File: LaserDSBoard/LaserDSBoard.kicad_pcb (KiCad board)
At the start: 2 copper layers, 110.5 x 77 mm, 185 parts, among them J1 JTAG, J10 Y LIMIT2, J11 LASER, J12 Y VREF, J13 X VREF, J14 Y1 MOTOR, J15 X MOTOR, J16 Y2 MOTOR, J2 USB, J3 POWER IN, J4 LASER P, J5 D SWITCH, J6 WATER FLOW, J7 X LIMIT1, J8 X LIMIT2, J9 Y LIMIT1, SW1 SW_PUSH, SW2 SWITCH_INV, U1 LD1117S33TR, U10 74HC08A, U11 ADUM1250, U12 TLP2355, U13 TLP2355, U14 TLP2355, U15 TLP2355, U16 TLP2355, U17 TLP2355, U18 74HC1G00, U19 MCP3425, U2 LD1117S33TR, U20 A4982SLPTR, U21 A4982SLPTR, U22 TLP2355, U3 STM32F20XR, U4 LD1117S50TR, U5 ADUM1250, U6 TLP627-4, U7 TLP627, U8 MCP44X1, U9 TLP627, X1 CRYSTAL_4PIN, X2 CRYSTAL

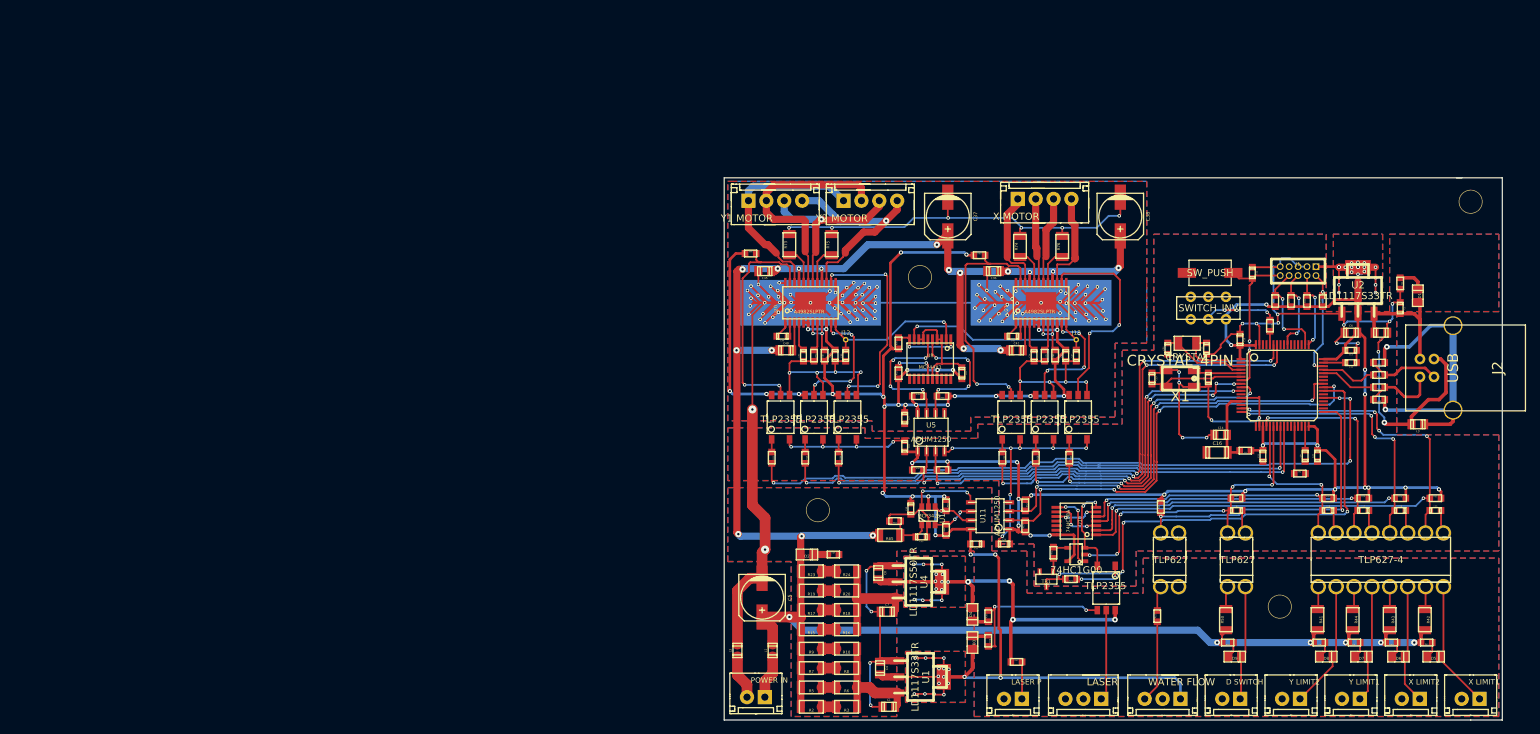
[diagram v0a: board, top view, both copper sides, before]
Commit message: DSコントロール基板改版
・2→4層化
・Y軸モータードライバ増設(1→2)
・コネクタ変更
・デジタルポテンショメータ変更
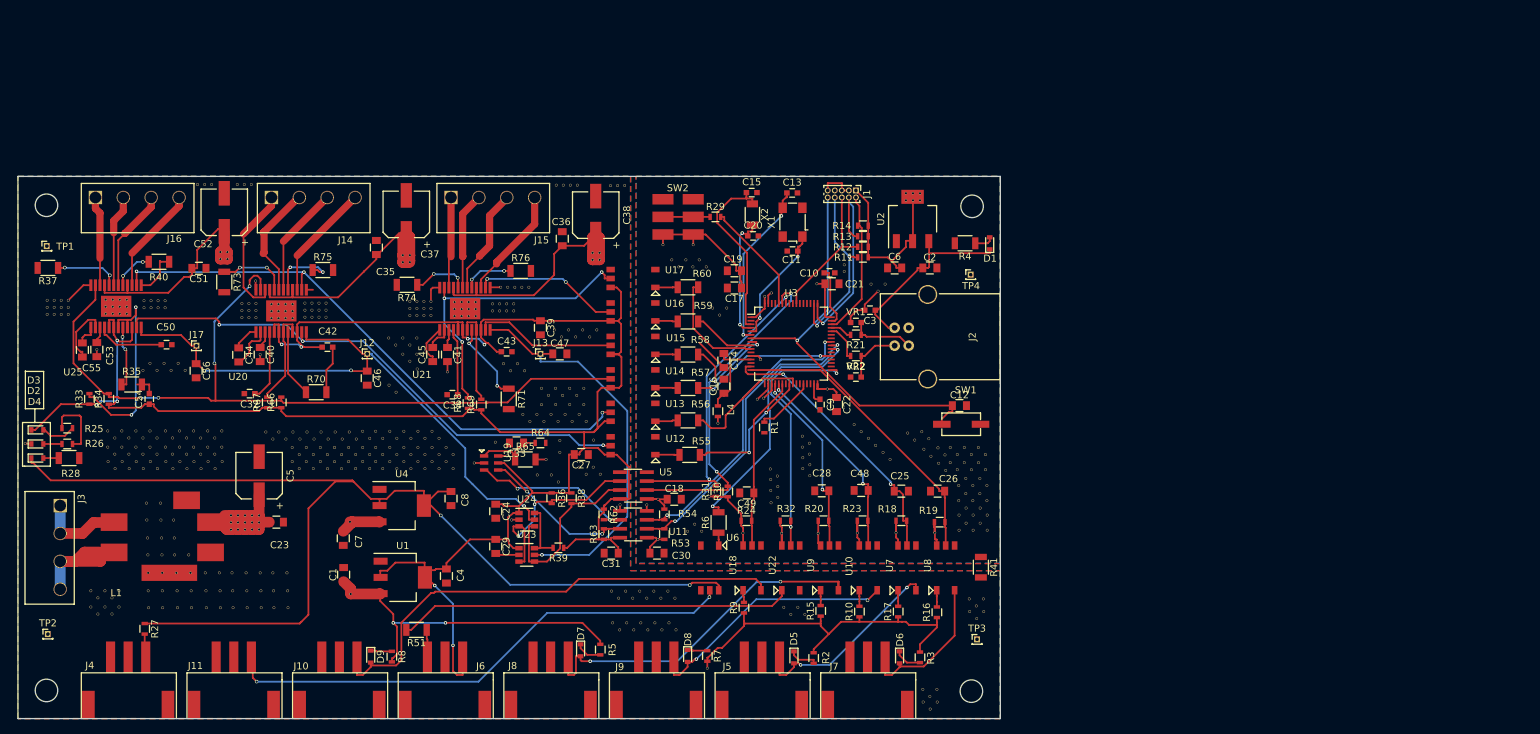
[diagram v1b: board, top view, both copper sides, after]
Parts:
- removed the ? at (245.3, 134.7)
- removed the ? at (338.0, 90.9)
- removed the ? at (310.9, 148.4)
- removed the ? at (259.8, 101.6)
- removed L2: BLM21SN300SN1D, C_0805
- removed L3: BLM21PG221SN1D, C_0805
- removed R42, R43, R44, R50: 1k, R_1206
- removed R45, R46, R47, R48, R49: 4k7, R_0603
- removed R52: 10k, R_0603
- removed R61: 100R, R_0603
- removed R72: 220R, R_0603
- removed TR1: BSH105, SOT-23
- added ?: , mylib:via, F.Cu at (201.2, 127.0)
- added ?: , mylib:via, F.Cu at (154.3, 148.6)
- added ?: , mylib:via, F.Cu at (243.2, 127.2)
- added ?: , mylib:via, F.Cu at (244.2, 128.2)
- added ?: , mylib:via, F.Cu at (244.2, 129.8)
- added ?: , mylib:via, F.Cu at (243.2, 128.8)
- added ?: , mylib:via, F.Cu at (243.1, 125.8)
- added ?: , mylib:via, F.Cu at (244.1, 126.8)
- added ?: , mylib:via, F.Cu at (254.6, 126.5)
- added ?: , mylib:via, F.Cu at (255.6, 127.5)
- added ?: , mylib:via, F.Cu at (253.5, 125.5)
- added ?: , mylib:via, F.Cu at (252.5, 124.5)
- added ?: , mylib:via, F.Cu at (156.3, 148.6)
- added ?: , mylib:via, F.Cu at (250.4, 122.5)
- added ?: , mylib:via, F.Cu at (251.4, 123.5)
- added ?: , mylib:via, F.Cu at (266.4, 136.6)
- added ?: , mylib:via, F.Cu at (268.4, 136.6)
- added ?: , mylib:via, F.Cu at (265.4, 137.6)
- added ?: , mylib:via, F.Cu at (267.4, 137.6)
- added ?: , mylib:via, F.Cu at (269.4, 137.6)
- added ?: , mylib:via, F.Cu at (269.4, 135.4)
- added ?: , mylib:via, F.Cu at (267.4, 135.4)
- added ?: , mylib:via, F.Cu at (265.4, 135.4)
- added ?: , mylib:via, F.Cu at (156.3, 146.2)
- added ?: , mylib:via, F.Cu at (268.4, 134.4)
- added ?: , mylib:via, F.Cu at (266.4, 134.4)
- added ?: , mylib:via, F.Cu at (266.3, 130.2)
- added ?: , mylib:via, F.Cu at (268.3, 130.2)
- added ?: , mylib:via, F.Cu at (265.3, 131.2)
- added ?: , mylib:via, F.Cu at (267.3, 131.2)
- added ?: , mylib:via, F.Cu at (269.3, 131.2)
- added ?: , mylib:via, F.Cu at (269.3, 133.3)
- added ?: , mylib:via, F.Cu at (267.3, 133.3)
- added ?: , mylib:via, F.Cu at (265.3, 133.3)
- added ?: , mylib:via, F.Cu at (154.3, 146.2)
- added ?: , mylib:via, F.Cu at (268.3, 132.3)
- added ?: , mylib:via, F.Cu at (266.3, 132.3)
- added ?: , mylib:via, F.Cu at (261.1, 124.5)
- added ?: , mylib:via, F.Cu at (244.1, 125.2)
- added ?: , mylib:via, F.Cu at (260.1, 123.5)
- added ?: , mylib:via, F.Cu at (243.1, 124.2)
- added ?: , mylib:via, F.Cu at (230.3, 106.0)
- added ?: , mylib:via, F.Cu at (232.3, 106.0)
- added ?: , mylib:via, F.Cu at (231.3, 107.0)
- added ?: , mylib:via, F.Cu at (228.4, 99.2)
- added ?: , mylib:via, F.Cu at (150.2, 146.2)
- added ?: , mylib:via, F.Cu at (229.4, 100.2)
- added ?: , mylib:via, F.Cu at (227.6, 100.2)
- added ?: , mylib:via, F.Cu at (225.6, 100.2)
- added ?: , mylib:via, F.Cu at (226.6, 99.2)
- added ?: , mylib:via, F.Cu at (224.6, 99.2)
- added ?: , mylib:via, F.Cu at (237.2, 113.3)
- added ?: , mylib:via, F.Cu at (263.4, 129.1)
- added ?: , mylib:via, F.Cu at (262.4, 128.1)
- added ?: , mylib:via, F.Cu at (227.8, 136.7)
- added ?: , mylib:via, F.Cu at (226.8, 137.7)
- added ?: , mylib:via, F.Cu at (152.2, 146.2)
- added ?: , mylib:via, F.Cu at (228.8, 137.7)
- added ?: , mylib:via, F.Cu at (264.1, 128.0)
- added ?: , mylib:via, F.Cu at (266.1, 128.0)
- added ?: , mylib:via, F.Cu at (268.1, 128.0)
- added ?: , mylib:via, F.Cu at (265.1, 128.9)
- added ?: , mylib:via, F.Cu at (267.1, 128.9)
- added ?: , mylib:via, F.Cu at (269.1, 128.9)
- added ?: , mylib:via, F.Cu at (249.1, 100.8)
- added ?: , mylib:via, F.Cu at (249.1, 99.8)
- added ?: , mylib:via, F.Cu at (252.8, 102.6)
- added ?: , mylib:via, F.Cu at (152.2, 148.6)
- added ?: , mylib:via, F.Cu at (254.8, 102.6)
- added ?: , mylib:via, F.Cu at (253.8, 103.6)
- added ?: , mylib:via, F.Cu at (238.7, 103.8)
- added ?: , mylib:via, F.Cu at (193.5, 128.8)
- added ?: , mylib:via, F.Cu at (191.5, 128.8)
- added ?: , mylib:via, F.Cu at (189.5, 128.8)
- added ?: , mylib:via, F.Cu at (187.5, 128.8)
- added ?: , mylib:via, F.Cu at (185.5, 128.8)
- added ?: , mylib:via, F.Cu at (183.5, 128.8)
- added ?: , mylib:via, F.Cu at (192.5, 127.8)
- added ?: , mylib:via, F.Cu at (150.2, 148.6)
- added ?: , mylib:via, F.Cu at (190.5, 127.8)
- added ?: , mylib:via, F.Cu at (188.5, 127.8)
- added ?: , mylib:via, F.Cu at (186.5, 127.8)
- added ?: , mylib:via, F.Cu at (184.5, 127.8)
- added ?: , mylib:via, F.Cu at (182.5, 127.8)
- added ?: , mylib:via, F.Cu at (170.7, 127.8)
- added ?: , mylib:via, F.Cu at (172.7, 127.8)
- added ?: , mylib:via, F.Cu at (174.7, 127.8)
- added ?: , mylib:via, F.Cu at (176.7, 127.8)
- added ?: , mylib:via, F.Cu at (178.7, 127.8)
- added ?: , mylib:via, F.Cu at (168.1, 148.6)
- added ?: , mylib:via, F.Cu at (180.7, 127.8)
- added ?: , mylib:via, F.Cu at (171.7, 128.8)
- added ?: , mylib:via, F.Cu at (173.7, 128.8)
- added ?: , mylib:via, F.Cu at (175.7, 128.8)
- added ?: , mylib:via, F.Cu at (177.7, 128.8)
- added ?: , mylib:via, F.Cu at (179.7, 128.8)
- added ?: , mylib:via, F.Cu at (181.7, 128.8)
- added ?: , mylib:via, F.Cu at (168.8, 123.6)
- added ?: , mylib:via, F.Cu at (170.8, 123.6)
- added ?: , mylib:via, F.Cu at (172.8, 123.6)
- added ?: , mylib:via, F.Cu at (170.1, 148.6)
- added ?: , mylib:via, F.Cu at (174.8, 123.6)
- added ?: , mylib:via, F.Cu at (176.8, 123.6)
- added ?: , mylib:via, F.Cu at (178.8, 123.6)
- added ?: , mylib:via, F.Cu at (169.8, 124.6)
- added ?: , mylib:via, F.Cu at (171.8, 124.6)
- added ?: , mylib:via, F.Cu at (173.8, 124.6)
- added ?: , mylib:via, F.Cu at (175.8, 124.6)
- added ?: , mylib:via, F.Cu at (177.8, 124.6)
- added ?: , mylib:via, F.Cu at (179.8, 124.6)
- added ?: , mylib:via, F.Cu at (167.9, 124.6)
- added ?: , mylib:via, F.Cu at (196.5, 128.0)
- added ?: , mylib:via, F.Cu at (170.0, 146.2)
- added ?: , mylib:via, F.Cu at (166.9, 123.6)
- added ?: , mylib:via, F.Cu at (213.4, 124.8)
- added ?: , mylib:via, F.Cu at (208.7, 124.8)
- added ?: , mylib:via, F.Cu at (208.7, 126.5)
- added ?: , mylib:via, F.Cu at (208.4, 130.7)
- added ?: , mylib:via, F.Cu at (201.8, 136.1)
- added ?: , mylib:via, F.Cu at (207.4, 129.7)
- added ?: , mylib:via, F.Cu at (205.4, 129.7)
- added ?: , mylib:via, F.Cu at (211.4, 128.6)
- added ?: , mylib:via, F.Cu at (213.4, 128.6)
- added ?: , mylib:via, F.Cu at (168.0, 146.2)
- added ?: , mylib:via, F.Cu at (212.4, 129.6)
- added ?: , mylib:via, F.Cu at (214.4, 129.6)
- added ?: , mylib:via, F.Cu at (203.7, 114.9)
- added ?: , mylib:via, F.Cu at (201.7, 114.9)
- added ?: , mylib:via, F.Cu at (202.7, 113.9)
- added ?: , mylib:via, F.Cu at (200.7, 113.9)
- added ?: , mylib:via, F.Cu at (207.9, 109.1)
- added ?: , mylib:via, F.Cu at (209.9, 109.1)
- added ?: , mylib:via, F.Cu at (211.9, 109.1)
- added ?: , mylib:via, F.Cu at (213.9, 109.1)
- added ?: , mylib:via, F.Cu at (169.9, 143.6)
- added ?: , mylib:via, F.Cu at (208.9, 110.1)
- added ?: , mylib:via, F.Cu at (210.9, 110.1)
- added ?: , mylib:via, F.Cu at (212.9, 110.1)
- added ?: , mylib:via, F.Cu at (266.9, 149.1)
- added ?: , mylib:via, F.Cu at (268.9, 149.1)
- added ?: , mylib:via, F.Cu at (267.9, 150.1)
- added ?: , mylib:via, F.Cu at (267.8, 148.3)
- added ?: , mylib:via, F.Cu at (268.8, 147.3)
- added ?: , mylib:via, F.Cu at (266.8, 147.3)
- added ?: , mylib:via, F.Cu at (260.2, 160.2)
- added ?: , mylib:via, F.Cu at (167.9, 143.6)
- added ?: , mylib:via, F.Cu at (262.2, 160.2)
- added ?: , mylib:via, F.Cu at (261.2, 161.2)
- added ?: , mylib:via, F.Cu at (261.2, 162.9)
- added ?: , mylib:via, F.Cu at (262.2, 161.9)
- added ?: , mylib:via, F.Cu at (260.2, 161.9)
- added ?: , mylib:via, F.Cu at (225.0, 147.2)
- added ?: , mylib:via, F.Cu at (223.0, 147.2)
- added ?: , mylib:via, F.Cu at (221.0, 147.2)
- added ?: , mylib:via, F.Cu at (219.0, 147.2)
- added ?: , mylib:via, F.Cu at (217.0, 147.2)
- added ?: , mylib:via, F.Cu at (166.1, 143.6)
- added ?: , mylib:via, F.Cu at (224.0, 146.2)
- added ?: , mylib:via, F.Cu at (222.0, 146.2)
- added ?: , mylib:via, F.Cu at (220.0, 146.2)
- added ?: , mylib:via, F.Cu at (218.0, 146.2)
- added ?: , mylib:via, F.Cu at (216.0, 146.2)
- added ?: , mylib:via, F.Cu at (212.4, 122.1)
- added ?: , mylib:via, F.Cu at (210.4, 122.1)
- added ?: , mylib:via, F.Cu at (208.4, 122.1)
- added ?: , mylib:via, F.Cu at (206.4, 122.1)
- added ?: , mylib:via, F.Cu at (204.4, 122.1)
- added ?: , mylib:via, F.Cu at (166.2, 146.2)
- added ?: , mylib:via, F.Cu at (211.4, 121.1)
- added ?: , mylib:via, F.Cu at (209.4, 121.1)
- added ?: , mylib:via, F.Cu at (207.4, 121.1)
- added ?: , mylib:via, F.Cu at (205.4, 121.1)
- added ?: , mylib:via, F.Cu at (203.4, 121.1)
- added ?: , mylib:via, F.Cu at (206.1, 119.7)
- added ?: , mylib:via, F.Cu at (208.1, 119.7)
- added ?: , mylib:via, F.Cu at (210.1, 119.7)
- added ?: , mylib:via, F.Cu at (212.1, 119.7)
- added ?: , mylib:via, F.Cu at (211.1, 118.4)
- added ?: , mylib:via, F.Cu at (166.2, 148.6)
- added ?: , mylib:via, F.Cu at (209.1, 118.4)
- added ?: , mylib:via, F.Cu at (207.1, 118.4)
- added ?: , mylib:via, F.Cu at (212.1, 117.4)
- added ?: , mylib:via, F.Cu at (210.1, 117.4)
- added ?: , mylib:via, F.Cu at (208.1, 117.4)
- added ?: , mylib:via, F.Cu at (206.1, 117.4)
- added ?: , mylib:via, F.Cu at (144.4, 123.5)
- added ?: , mylib:via, F.Cu at (146.4, 123.5)
- added ?: , mylib:via, F.Cu at (148.4, 123.5)
- added ?: , mylib:via, F.Cu at (150.4, 123.5)
- added ?: , mylib:via, F.Cu at (158.4, 148.6)
- added ?: , mylib:via, F.Cu at (145.4, 124.5)
- added ?: , mylib:via, F.Cu at (147.4, 124.5)
- added ?: , mylib:via, F.Cu at (149.4, 124.5)
- added ?: , mylib:via, F.Cu at (151.4, 124.5)
- added ?: , mylib:via, F.Cu at (151.4, 126.8)
- added ?: , mylib:via, F.Cu at (149.4, 126.8)
- added ?: , mylib:via, F.Cu at (147.4, 126.8)
- added ?: , mylib:via, F.Cu at (145.4, 126.8)
- added ?: , mylib:via, F.Cu at (150.4, 125.8)
- added ?: , mylib:via, F.Cu at (148.4, 125.8)
- added ?: , mylib:via, F.Cu at (160.4, 148.6)
- added ?: , mylib:via, F.Cu at (146.4, 125.8)
- added ?: , mylib:via, F.Cu at (144.4, 125.8)
- added ?: , mylib:via, F.Cu at (156.2, 143.6)
- added ?: , mylib:via, F.Cu at (154.2, 143.6)
- added ?: , mylib:via, F.Cu at (152.2, 143.6)
- added ?: , mylib:via, F.Cu at (150.2, 143.6)
- added ?: , mylib:via, F.Cu at (142.1, 148.4)
- added ?: , mylib:via, F.Cu at (144.1, 148.4)
- added ?: , mylib:via, F.Cu at (146.1, 148.4)
- added ?: , mylib:via, F.Cu at (143.1, 149.4)
- added ?: , mylib:via, F.Cu at (160.4, 146.2)
- added ?: , mylib:via, F.Cu at (145.1, 149.4)
- added ?: , mylib:via, F.Cu at (145.1, 147.2)
- added ?: , mylib:via, F.Cu at (143.1, 147.2)
- added ?: , mylib:via, F.Cu at (146.1, 146.2)
- added ?: , mylib:via, F.Cu at (144.1, 146.2)
- added ?: , mylib:via, F.Cu at (142.1, 146.2)
- added ?: , mylib:via, F.Cu at (152.7, 125.8)
- added ?: , mylib:via, F.Cu at (154.7, 125.8)
- added ?: , mylib:via, F.Cu at (156.7, 125.8)
- added ?: , mylib:via, F.Cu at (158.7, 125.8)
- added ?: , mylib:via, F.Cu at (199.5, 125.0)
- added ?: , mylib:via, F.Cu at (158.4, 146.2)
- added ?: , mylib:via, F.Cu at (160.7, 125.8)
- added ?: , mylib:via, F.Cu at (153.7, 126.8)
- added ?: , mylib:via, F.Cu at (155.7, 126.8)
- added ?: , mylib:via, F.Cu at (157.7, 126.8)
- added ?: , mylib:via, F.Cu at (159.7, 126.8)
- added ?: , mylib:via, F.Cu at (159.7, 124.5)
- added ?: , mylib:via, F.Cu at (157.7, 124.5)
- added ?: , mylib:via, F.Cu at (155.7, 124.5)
- added ?: , mylib:via, F.Cu at (153.7, 124.5)
- added ?: , mylib:via, F.Cu at (160.7, 123.5)
- added ?: , mylib:via, F.Cu at (160.3, 143.6)
- added ?: , mylib:via, F.Cu at (158.7, 123.5)
- added ?: , mylib:via, F.Cu at (156.7, 123.5)
- added ?: , mylib:via, F.Cu at (154.7, 123.5)
- added ?: , mylib:via, F.Cu at (152.7, 123.5)
- added ?: , mylib:via, F.Cu at (184.3, 110.2)
- added ?: , mylib:via, F.Cu at (186.3, 110.2)
- added ?: , mylib:via, F.Cu at (188.3, 110.2)
- added ?: , mylib:via, F.Cu at (185.3, 111.2)
- added ?: , mylib:via, F.Cu at (187.3, 111.2)
- added ?: , mylib:via, F.Cu at (187.3, 113.5)
- added ?: , mylib:via, F.Cu at (158.3, 143.6)
- added ?: , mylib:via, F.Cu at (188.3, 112.5)
- added ?: , mylib:via, F.Cu at (186.3, 112.5)
- added ?: , mylib:via, F.Cu at (184.4, 117.0)
- added ?: , mylib:via, F.Cu at (185.4, 118.0)
- added ?: , mylib:via, F.Cu at (188.4, 114.7)
- added ?: , mylib:via, F.Cu at (216.2, 150.7)
- added ?: , mylib:via, F.Cu at (218.2, 150.7)
- added ?: , mylib:via, F.Cu at (220.2, 150.7)
- added ?: , mylib:via, F.Cu at (222.2, 150.7)
- added ?: , mylib:via, F.Cu at (224.2, 150.7)
- added ?: , mylib:via, F.Cu at (162.1, 143.6)
- added ?: , mylib:via, F.Cu at (180.7, 123.5)
- added ?: , mylib:via, F.Cu at (217.2, 151.7)
- added ?: , mylib:via, F.Cu at (219.2, 151.7)
- added ?: , mylib:via, F.Cu at (221.2, 151.7)
- added ?: , mylib:via, F.Cu at (223.2, 151.7)
- added ?: , mylib:via, F.Cu at (225.2, 151.7)
- added ?: , mylib:via, F.Cu at (181.7, 124.5)
- added ?: , mylib:via, F.Cu at (181.7, 126.8)
- added ?: , mylib:via, F.Cu at (179.7, 126.8)
- added ?: , mylib:via, F.Cu at (177.7, 126.8)
- added ?: , mylib:via, F.Cu at (164.1, 143.6)
- added ?: , mylib:via, F.Cu at (175.7, 126.8)
- added ?: , mylib:via, F.Cu at (173.7, 126.8)
- added ?: , mylib:via, F.Cu at (171.7, 126.8)
- added ?: , mylib:via, F.Cu at (180.7, 125.8)
- added ?: , mylib:via, F.Cu at (178.7, 125.8)
- added ?: , mylib:via, F.Cu at (176.7, 125.8)
- added ?: , mylib:via, F.Cu at (174.7, 125.8)
- added ?: , mylib:via, F.Cu at (172.7, 125.8)
- added ?: , mylib:via, F.Cu at (170.7, 125.8)
- added ?: , mylib:via, F.Cu at (182.5, 125.8)
- added ?: , mylib:via, F.Cu at (162.2, 146.2)
- added ?: , mylib:via, F.Cu at (184.5, 125.8)
- added ?: , mylib:via, F.Cu at (186.5, 125.8)
- added ?: , mylib:via, F.Cu at (188.5, 125.8)
- added ?: , mylib:via, F.Cu at (190.5, 125.8)
- added ?: , mylib:via, F.Cu at (192.5, 125.8)
- added ?: , mylib:via, F.Cu at (183.5, 126.8)
- added ?: , mylib:via, F.Cu at (185.5, 126.8)
- added ?: , mylib:via, F.Cu at (187.5, 126.8)
- added ?: , mylib:via, F.Cu at (189.5, 126.8)
- added ?: , mylib:via, F.Cu at (191.5, 126.8)
- added ?: , mylib:via, F.Cu at (164.2, 146.2)
- added ?: , mylib:via, F.Cu at (193.5, 126.8)
- added ?: , mylib:via, F.Cu at (151.4, 114.8)
- added ?: , mylib:via, F.Cu at (191.5, 124.5)
- added ?: , mylib:via, F.Cu at (189.5, 124.5)
- added ?: , mylib:via, F.Cu at (187.5, 124.5)
- added ?: , mylib:via, F.Cu at (185.5, 124.5)
- added ?: , mylib:via, F.Cu at (183.5, 124.5)
- added ?: , mylib:via, F.Cu at (155.4, 114.8)
- added ?: , mylib:via, F.Cu at (153.4, 114.8)
- added ?: , mylib:via, F.Cu at (149.4, 114.8)
- added ?: , mylib:via, F.Cu at (164.2, 148.6)
- added ?: , mylib:via, F.Cu at (190.5, 123.5)
- added ?: , mylib:via, F.Cu at (188.5, 123.5)
- added ?: , mylib:via, F.Cu at (186.5, 123.5)
- added ?: , mylib:via, F.Cu at (184.5, 123.5)
- added ?: , mylib:via, F.Cu at (182.5, 123.5)
- added ?: , mylib:via, F.Cu at (154.4, 113.8)
- added ?: , mylib:via, F.Cu at (152.4, 113.8)
- added ?: , mylib:via, F.Cu at (150.4, 113.8)
- added ?: , mylib:via, F.Cu at (259.8, 90.7)
- added ?: , mylib:via, F.Cu at (258.8, 90.7)
- added ?: , mylib:via, F.Cu at (162.2, 148.6)
- added ?: , mylib:via, F.Cu at (257.8, 90.7)
- added ?: , mylib:via, F.Cu at (246.7, 117.5)
- added ?: , mylib:via, F.Cu at (245.2, 102.5)
- added ?: , mylib:via, F.Cu at (229.8, 132.8)
- added ?: , mylib:via, F.Cu at (222.6, 133.2)
- added ?: , mylib:via, F.Cu at (261.9, 137.9)
- added ?: , mylib:via, F.Cu at (250.9, 137.9)
- added ?: , mylib:via, F.Cu at (259.8, 89.7)
- added ?: , mylib:via, F.Cu at (258.8, 89.7)
- added ?: , mylib:via, F.Cu at (257.8, 89.7)
- added ?: , mylib:via, F.Cu at (153.9, 141.1)
- added ?: , mylib:via, F.Cu at (237.6, 118.8)
- added ?: , mylib:via, F.Cu at (231.1, 122.3)
- added ?: , mylib:via, F.Cu at (237.8, 104.3)
- added ?: , mylib:via, F.Cu at (227.6, 97.0)
- added ?: , mylib:via, F.Cu at (223.3, 97.0)
- added ?: , mylib:via, F.Cu at (222.6, 138.8)
- added ?: , mylib:via, F.Cu at (256.4, 137.9)
- added ?: , mylib:via, F.Cu at (245.3, 138.0)
- added ?: , mylib:via, F.Cu at (240.2, 138.0)
- added ?: , mylib:via, F.Cu at (234.7, 137.9)
- added ?: , mylib:via, F.Cu at (161.9, 135.4)
- added ?: , mylib:via, F.Cu at (155.9, 141.1)
- added ?: , mylib:via, F.Cu at (221.0, 133.9)
- added ?: , mylib:via, F.Cu at (236.7, 119.0)
- added ?: , mylib:via, F.Cu at (269.1, 126.8)
- added ?: , mylib:via, F.Cu at (267.1, 126.8)
- added ?: , mylib:via, F.Cu at (265.1, 126.8)
- added ?: , mylib:via, F.Cu at (268.1, 125.8)
- added ?: , mylib:via, F.Cu at (266.1, 125.8)
- added ?: , mylib:via, F.Cu at (187.3, 99.5)
- added ?: , mylib:via, F.Cu at (186.3, 99.5)
- added ?: , mylib:via, F.Cu at (214.3, 99.2)
- added ?: , mylib:via, F.Cu at (153.9, 138.7)
- added ?: , mylib:via, F.Cu at (213.3, 99.2)
- added ?: , mylib:via, F.Cu at (165.9, 137.4)
- added ?: , mylib:via, F.Cu at (164.9, 137.4)
- added ?: , mylib:via, F.Cu at (163.9, 137.4)
- added ?: , mylib:via, F.Cu at (132.8, 125.2)
- added ?: , mylib:via, F.Cu at (161.4, 99.0)
- added ?: , mylib:via, F.Cu at (160.4, 99.0)
- added ?: , mylib:via, F.Cu at (187.3, 98.5)
- added ?: , mylib:via, F.Cu at (186.3, 98.5)
- added ?: , mylib:via, F.Cu at (214.3, 98.2)
- added ?: , mylib:via, F.Cu at (153.8, 136.1)
- added ?: , mylib:via, F.Cu at (213.3, 98.2)
- added ?: , mylib:via, F.Cu at (165.9, 136.4)
- added ?: , mylib:via, F.Cu at (164.9, 136.4)
- added ?: , mylib:via, F.Cu at (163.9, 136.4)
- added ?: , mylib:via, F.Cu at (142.9, 111.9)
- added ?: , mylib:via, F.Cu at (166.1, 112.6)
- added ?: , mylib:via, F.Cu at (192.7, 115.0)
- added ?: , mylib:via, F.Cu at (161.4, 98.0)
- added ?: , mylib:via, F.Cu at (160.4, 98.0)
- added ?: , mylib:via, F.Cu at (178.9, 146.6)
- added ?: , mylib:via, F.Cu at (150.0, 136.1)
- added ?: , mylib:via, F.Cu at (206.7, 127.5)
- added ?: , mylib:via, F.Cu at (178.8, 136.3)
- added ?: , mylib:via, F.Cu at (229.6, 157.2)
- added ?: , mylib:via, F.Cu at (165.9, 135.4)
- added ?: , mylib:via, F.Cu at (164.9, 135.4)
- added ?: , mylib:via, F.Cu at (163.9, 135.4)
- added ?: , mylib:via, F.Cu at (202.1, 106.4)
- added ?: , mylib:via, F.Cu at (201.1, 106.4)
- added ?: , mylib:via, F.Cu at (200.1, 106.4)
- added ?: , mylib:via, F.Cu at (199.1, 106.4)
- added ?: , mylib:via, F.Cu at (152.0, 136.1)
- added ?: , mylib:via, F.Cu at (190.3, 107.0)
- added ?: , mylib:via, F.Cu at (189.3, 107.0)
- added ?: , mylib:via, F.Cu at (188.3, 107.0)
- added ?: , mylib:via, F.Cu at (187.3, 107.0)
- added ?: , mylib:via, F.Cu at (175.4, 107.3)
- added ?: , mylib:via, F.Cu at (174.4, 107.3)
- added ?: , mylib:via, F.Cu at (173.4, 107.3)
- added ?: , mylib:via, F.Cu at (172.4, 107.3)
- added ?: , mylib:via, F.Cu at (165.5, 107.3)
- added ?: , mylib:via, F.Cu at (164.5, 107.3)
- added ?: , mylib:via, F.Cu at (151.9, 133.7)
- added ?: , mylib:via, F.Cu at (163.5, 107.3)
- added ?: , mylib:via, F.Cu at (204.2, 103.0)
- added ?: , mylib:via, F.Cu at (203.2, 103.0)
- added ?: , mylib:via, F.Cu at (202.2, 103.0)
- added ?: , mylib:via, F.Cu at (201.2, 103.0)
- added ?: , mylib:via, F.Cu at (200.2, 103.0)
- added ?: , mylib:via, F.Cu at (202.1, 105.4)
- added ?: , mylib:via, F.Cu at (201.1, 105.4)
- added ?: , mylib:via, F.Cu at (200.1, 105.4)
- added ?: , mylib:via, F.Cu at (199.1, 105.4)
- added ?: , mylib:via, F.Cu at (149.9, 133.7)
- added ?: , mylib:via, F.Cu at (190.3, 106.0)
- added ?: , mylib:via, F.Cu at (189.3, 106.0)
- added ?: , mylib:via, F.Cu at (188.3, 106.0)
- added ?: , mylib:via, F.Cu at (187.3, 106.0)
- added ?: , mylib:via, F.Cu at (175.4, 106.3)
- added ?: , mylib:via, F.Cu at (174.4, 106.3)
- added ?: , mylib:via, F.Cu at (173.4, 106.3)
- added ?: , mylib:via, F.Cu at (172.4, 106.3)
- added ?: , mylib:via, F.Cu at (165.5, 106.3)
- added ?: , mylib:via, F.Cu at (164.5, 106.3)
- added ?: , mylib:via, F.Cu at (150.1, 138.7)
- added ?: , mylib:via, F.Cu at (163.5, 106.3)
- added ?: , mylib:via, F.Cu at (264.1, 125.8)
- added ?: , mylib:via, F.Cu at (190.3, 105.0)
- added ?: , mylib:via, F.Cu at (189.3, 105.0)
- added ?: , mylib:via, F.Cu at (188.3, 105.0)
- added ?: , mylib:via, F.Cu at (187.3, 105.0)
- added ?: , mylib:via, F.Cu at (175.4, 105.3)
- added ?: , mylib:via, F.Cu at (174.4, 105.3)
- added ?: , mylib:via, F.Cu at (173.4, 105.3)
- added ?: , mylib:via, F.Cu at (172.4, 105.3)
- added ?: , mylib:via, F.Cu at (152.1, 138.7)
- added ?: , mylib:via, F.Cu at (165.5, 105.3)
- added ?: , mylib:via, F.Cu at (164.5, 105.3)
- added ?: , mylib:via, F.Cu at (163.5, 105.3)
- added ?: , mylib:via, F.Cu at (138.8, 106.9)
- added ?: , mylib:via, F.Cu at (137.8, 106.9)
- added ?: , mylib:via, F.Cu at (136.8, 106.9)
- added ?: , mylib:via, F.Cu at (135.8, 106.9)
- added ?: , mylib:via, F.Cu at (196.7, 107.2)
- added ?: , mylib:via, F.Cu at (195.7, 107.2)
- added ?: , mylib:via, F.Cu at (194.7, 107.2)
- added ?: , mylib:via, F.Cu at (152.2, 141.1)
- added ?: , mylib:via, F.Cu at (193.7, 107.2)
- added ?: , mylib:via, F.Cu at (170.7, 107.5)
- added ?: , mylib:via, F.Cu at (169.7, 107.5)
- added ?: , mylib:via, F.Cu at (168.7, 107.5)
- added ?: , mylib:via, F.Cu at (167.7, 107.5)
- added ?: , mylib:via, F.Cu at (147.2, 106.8)
- added ?: , mylib:via, F.Cu at (146.2, 106.8)
- added ?: , mylib:via, F.Cu at (145.2, 106.8)
- added ?: , mylib:via, F.Cu at (144.2, 106.8)
- added ?: , mylib:via, F.Cu at (152.6, 106.0)
- added ?: , mylib:via, F.Cu at (162.9, 135.4)
- added ?: , mylib:via, F.Cu at (150.2, 141.1)
- added ?: , mylib:via, F.Cu at (151.6, 106.0)
- added ?: , mylib:via, F.Cu at (150.6, 106.0)
- added ?: , mylib:via, F.Cu at (149.6, 106.0)
- added ?: , mylib:via, F.Cu at (138.8, 105.9)
- added ?: , mylib:via, F.Cu at (137.8, 105.9)
- added ?: , mylib:via, F.Cu at (136.8, 105.9)
- added ?: , mylib:via, F.Cu at (135.8, 105.9)
- added ?: , mylib:via, F.Cu at (196.7, 106.2)
- added ?: , mylib:via, F.Cu at (195.7, 106.2)
- added ?: , mylib:via, F.Cu at (194.7, 106.2)
- added ?: , mylib:via, F.Cu at (243.4, 149.5)
- added ?: , mylib:via, F.Cu at (193.7, 106.2)
- added ?: , mylib:via, F.Cu at (170.7, 106.5)
- added ?: , mylib:via, F.Cu at (169.7, 106.5)
- added ?: , mylib:via, F.Cu at (168.7, 106.5)
- added ?: , mylib:via, F.Cu at (167.7, 106.5)
- added ?: , mylib:via, F.Cu at (147.2, 105.8)
- added ?: , mylib:via, F.Cu at (146.2, 105.8)
- added ?: , mylib:via, F.Cu at (145.2, 105.8)
- added ?: , mylib:via, F.Cu at (144.2, 105.8)
- added ?: , mylib:via, F.Cu at (152.6, 105.0)
- added ?: , mylib:via, F.Cu at (241.4, 149.5)
- added ?: , mylib:via, F.Cu at (151.6, 105.0)
- added ?: , mylib:via, F.Cu at (150.6, 105.0)
- added ?: , mylib:via, F.Cu at (149.6, 105.0)
- added ?: , mylib:via, F.Cu at (138.8, 104.9)
- added ?: , mylib:via, F.Cu at (137.8, 104.9)
- added ?: , mylib:via, F.Cu at (136.8, 104.9)
- added ?: , mylib:via, F.Cu at (135.8, 104.9)
- added ?: , mylib:via, F.Cu at (196.7, 105.2)
- added ?: , mylib:via, F.Cu at (195.7, 105.2)
- added ?: , mylib:via, F.Cu at (194.7, 105.2)
- added ?: , mylib:via, F.Cu at (242.4, 148.5)
- added ?: , mylib:via, F.Cu at (193.7, 105.2)
- added ?: , mylib:via, F.Cu at (170.7, 105.5)
- added ?: , mylib:via, F.Cu at (169.7, 105.5)
- added ?: , mylib:via, F.Cu at (168.7, 105.5)
- added ?: , mylib:via, F.Cu at (167.7, 105.5)
- added ?: , mylib:via, F.Cu at (147.2, 104.8)
- added ?: , mylib:via, F.Cu at (146.2, 104.8)
- added ?: , mylib:via, F.Cu at (145.2, 104.8)
- added ?: , mylib:via, F.Cu at (144.2, 104.8)
- added ?: MountingHole_3.2mm_M3, Mounting_Holes:MountingHole_3.2mm_M3, F.Cu at (135.8, 91.4)
- added ?: , mylib:via, F.Cu at (240.4, 148.5)
- added ?: , Mounting_Holes:MountingHole_3.2mm_M3, F.Cu at (135.8, 160.3)
- added ?: MountingHole_3.2mm_M3, Mounting_Holes:MountingHole_3.2mm_M3, F.Cu at (267.2, 91.5)
- added ?: MountingHole_3.2mm_M3, Mounting_Holes:MountingHole_3.2mm_M3, F.Cu at (267.1, 160.4)
- added ?: , mylib:via, F.Cu at (159.7, 128.8)
- added ?: , mylib:via, F.Cu at (157.7, 128.8)
- added ?: , mylib:via, F.Cu at (155.7, 128.8)
- added ?: , mylib:via, F.Cu at (153.7, 128.8)
- added ?: , mylib:via, F.Cu at (160.7, 127.8)
- added ?: , mylib:via, F.Cu at (161.9, 136.4)
- added ?: , mylib:via, F.Cu at (158.7, 127.8)
- added ?: , mylib:via, F.Cu at (156.7, 127.8)
- added ?: , mylib:via, F.Cu at (154.7, 127.8)
- added ?: , mylib:via, F.Cu at (152.7, 127.8)
- added ?: , mylib:via, F.Cu at (144.5, 127.8)
- added ?: , mylib:via, F.Cu at (146.5, 127.8)
- added ?: , mylib:via, F.Cu at (148.5, 127.8)
- added ?: , mylib:via, F.Cu at (150.5, 127.8)
- added ?: , mylib:via, F.Cu at (145.5, 128.8)
- added ?: , mylib:via, F.Cu at (147.5, 128.8)
- added ?: , mylib:via, F.Cu at (162.9, 136.4)
- added ?: , mylib:via, F.Cu at (149.5, 128.8)
- added ?: , mylib:via, F.Cu at (151.5, 128.8)
- added ?: , mylib:via, F.Cu at (165.4, 102.2)
- added ?: , mylib:via, F.Cu at (217.2, 133.9)
- added ?: , mylib:via, F.Cu at (262.4, 125.8)
- added ?: , mylib:via, F.Cu at (263.4, 126.8)
- added ?: , mylib:via, F.Cu at (261.4, 127.0)
- added ?: , mylib:via, F.Cu at (260.4, 126.0)
- added ?: , mylib:via, F.Cu at (258.1, 123.8)
- added ?: , mylib:via, F.Cu at (259.1, 124.8)
- added ?: , mylib:via, F.Cu at (161.9, 137.4)
- added ?: , mylib:via, F.Cu at (159.2, 88.5)
- added ?: , mylib:via, F.Cu at (158.2, 88.5)
- added ?: , mylib:via, F.Cu at (157.2, 88.5)
- added ?: , mylib:via, F.Cu at (162.8, 88.5)
- added ?: , mylib:via, F.Cu at (163.8, 88.5)
- added ?: , mylib:via, F.Cu at (164.8, 88.5)
- added ?: , mylib:via, F.Cu at (217.8, 88.6)
- added ?: , mylib:via, F.Cu at (216.8, 88.6)
- added ?: , mylib:via, F.Cu at (215.8, 88.6)
- added ?: , mylib:via, F.Cu at (208.2, 88.5)
- added ?: , mylib:via, F.Cu at (162.9, 137.4)
- added ?: , mylib:via, F.Cu at (209.2, 88.5)
- added ?: , mylib:via, F.Cu at (210.2, 88.5)
- added ?: , mylib:via, F.Cu at (211.2, 88.5)
- added ?: , mylib:via, F.Cu at (238.7, 133.7)
- added ?: , mylib:via, F.Cu at (239.6, 129.8)
- added ?: , mylib:via, F.Cu at (238.6, 128.8)
- added ?: , mylib:via, F.Cu at (238.6, 131.9)
- added ?: , mylib:via, F.Cu at (239.6, 132.9)
- added ?: , mylib:via, F.Cu at (239.6, 131.3)
- added ?: , mylib:via, F.Cu at (238.6, 130.3)
- added C48: 0u1, Capacitors_SMD:C_0805, F.Cu at (251.4, 131.9)
- added C49: 0u1, Capacitors_SMD:C_0805, F.Cu at (235.2, 132.2)
- added C50: 0u22, Capacitors_SMD:C_0603, F.Cu at (152.8, 111.2)
- added C51: 0u1, Capacitors_SMD:C_0805, F.Cu at (157.4, 100.3)
- added C52: 100u, Capacitors_SMD:CP_Elec_6.3x7.7, F.Cu at (161.0, 92.4)
- added C53: 0u1, Capacitors_SMD:C_0805, F.Cu at (142.9, 111.9)
- added C54: 0u22, Capacitors_SMD:C_0603, F.Cu at (150.3, 118.9)
- added C55: 0u1, Capacitors_SMD:C_0805, F.Cu at (140.8, 112.0)
- added C56: 0u1, Capacitors_SMD:C_0805, F.Cu at (157.0, 114.9)
- added G***: LOGO, logo:smartDIYslogo, B.Cu at (148.9, 160.8)
- added J17: Y VREF, Pin_Headers:Pin_Header_Straight_1x01_Pitch1.00mm, F.Cu at (157.1, 111.3)
- added TP1: CP-10, Pin_Headers:Pin_Header_Straight_1x01_Pitch1.00mm, F.Cu at (135.8, 97.2)
- added TP2: CP-10, Pin_Headers:Pin_Header_Straight_1x01_Pitch1.00mm, F.Cu at (135.9, 152.3)
- added TP3: CP-10, Pin_Headers:Pin_Header_Straight_1x01_Pitch1.00mm, F.Cu at (267.9, 153.1)
- added TP4: CP-10, Pin_Headers:Pin_Header_Straight_1x01_Pitch1.00mm, F.Cu at (267.0, 101.2)
- added U23: TPL0401A, TO_SOT_Packages_SMD:SOT-23-6, F.Cu at (203.9, 141.1)
- added U24: TPL0401B, TO_SOT_Packages_SMD:SOT-23-6, F.Cu at (203.9, 136.1)
- added U25: A4982SLPTR, mylib:A4982SLPTR, F.Cu at (142.1, 108.8)
- C1, C14, C2, C35, C36, C4, C40, C41, C6, C7, C8: footprint C_0805 -> Capacitors_SMD:C_0805
- C10, C11, C13, C15, C20, C3, C32, C34, C42, C43, C9: footprint C_0603 -> Capacitors_SMD:C_0603
- C12, C17, C18, C19, C21, C22, C23, C24, C25, C26, C27, C28, C29, C30, C31, C33, C39, C44, C45, C46, C47: footprint C_0603 -> Capacitors_SMD:C_0805
- C16: footprint C_1206 -> Capacitors_SMD:C_0805
- C37, C38, C5: footprint C_ELEC_6.3x7.7 -> Capacitors_SMD:CP_Elec_6.3x7.7
- D1, D2, D3, D4, D5, D6, D7, D8, D9: footprint D_0805 -> Diodes_SMD:D_0603
- J1: footprint MICRO_5x2 -> Pin_Headers:Pin_Header_Straight_2x05_Pitch1.00mm
- J10: value Y LIMIT2 -> D SWITCH; footprint B2B-XH-A -> mylib:S3B-XH-SM4-TB
- J11, J6: footprint B3B-XH-A -> mylib:S3B-XH-SM4-TB
- J12, J13: footprint Vref -> Pin_Headers:Pin_Header_Straight_1x01_Pitch1.00mm
- J14, J15, J16: footprint B4B-XH-A -> mylib:VH-4
- J2: footprint USB_B -> mylib:USB_B
- J3: footprint B2B-XH-A -> mylib:VH-4
- J4: footprint B2B-XH-A -> mylib:S3B-XH-SM4-TB
- J5: value D SWITCH -> X LIMIT1; footprint B2B-XH-A -> mylib:S3B-XH-SM4-TB
- J7: value X LIMIT1 -> X LIMIT2; footprint B2B-XH-A -> mylib:S3B-XH-SM4-TB
- J8: value X LIMIT2 -> Y LIMIT1; footprint B2B-XH-A -> mylib:S3B-XH-SM4-TB
- J9: value Y LIMIT1 -> Y LIMIT2; footprint B2B-XH-A -> mylib:S3B-XH-SM4-TB
- L1: value BLM21SN300SN1D -> BNX024H01; footprint C_0805 -> mylib:BNX024H01
- L4: value Ferrite bead -> LI0603G221R-10; footprint R_0603 -> Resistors_SMD:R_0603
- R1, R11, R12, R13, R14, R21, R22, R25, R26, R27, R29, R30, R31, R39, R53, R54, R62, R63, R64, R66, R67, R68, R69: footprint R_0603 -> Resistors_SMD:R_0603
- R10, R15, R16, R17, R18, R19, R20, R23, R24, R9: value 220R -> 1k; footprint R_1206 -> Resistors_SMD:R_0603
- R2, R3, R5, R7, R8: value 220R -> 4k7; footprint R_1206 -> Resistors_SMD:R_0603
- R28, R4, R51, R55, R56, R57, R58, R59, R60, R70, R71: footprint R_0603 -> Resistors_SMD:R_1206
- R32, R36, R38: value 4k7 -> 1k; footprint R_0603 -> Resistors_SMD:R_0603
- R33: value 4k7 -> 10k; footprint R_0603 -> Resistors_SMD:R_0603
- R34: value 4k7 -> 100k; footprint R_0603 -> Resistors_SMD:R_0603
- R35: value 4k7 -> 0R; footprint R_0603 -> Resistors_SMD:R_1206
- R37, R40: value 4k7 -> 0R1; footprint R_0603 -> Resistors_SMD:R_1206
- R41: value 1k -> 0R; footprint R_1206 -> Resistors_SMD:R_1206
- R6, R65, R73, R74, R75, R76: footprint R_1206 -> Resistors_SMD:R_1206
- SW1: value SW_PUSH -> DHT-1163S; footprint DHT-1163S -> mylib:DHT-1163S
- SW2: value SWITCH_INV -> SSSS213202; footprint MS-22D18 -> mylib:SSSS213202
- U1, U2: value LD1117S33TR -> LD1117S; footprint SOT-223 -> mylib:LD1117S33TR
- U10: value 74HC08A -> TLP2355; footprint TSSOP-14 -> mylib:TLP2355
- U11, U5: footprint SOIC-8 -> mylib:ADUM1250
- U12, U13, U14, U15, U16, U17, U22: footprint TLP2355 -> mylib:TLP2355
- U18: value 74HC1G00 -> TLP2355; footprint TSOP-5 -> mylib:TLP2355
- U19: footprint SOT23_6 -> mylib:MCP3425
- U20, U21: footprint TSSOP-24-thin_pads -> mylib:A4982SLPTR
- U3: footprint LQFP64 -> Housings_QFP:LQFP-64_10x10mm_Pitch0.5mm
- U4: value LD1117S50TR -> LD1117S; footprint SOT-223 -> mylib:LD1117S33TR
- U6: value TLP627-4 -> TLP2355; footprint TLP627-4 -> mylib:TLP2355
- U7, U9: value TLP627 -> TLP2355; footprint TLP627 -> mylib:TLP2355
- U8: value MCP44X1 -> TLP2355; footprint TSSOP-20 -> mylib:TLP2355
- VR1, VR2: footprint R_0603 -> Capacitors_SMD:C_0603
- X1: value CRYSTAL_4PIN -> 7B-25.000MAAJ-T; footprint Xtal_5x3.2 -> Oscillators:Oscillator_SMD_Fordahl_DFAS15-4pin_5.0x3.2mm
- X2: value CRYSTAL -> 9HT10-32.768KDZY-T; footprint 2-SMD -> Capacitors_SMD:C_1206
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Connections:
- net N-0000064 renamed Y_STEP_A
- net N-0000072 renamed Y_DIR_A
- C1 pad 1: N-00000129 -> A+12V
- C1 pad 2: DGND -> GNDA
- C10 pad 2: GND -> GNDD
- C11 pad 2: GND -> GNDD
- C12 pad 2: GND -> GNDD
- C13 pad 2: GND -> GNDD
- C14 pad 2: GND -> GNDD
- C15 pad 2: GND -> GNDD
- C16 pad 2: GND -> GNDD
- C17 pad 1: +3.3V -> D+3.3V
- C17 pad 2: GND -> GNDD
- C18 pad 1: +3.3V -> D+3.3V
- C18 pad 2: GND -> GNDD
- C19 pad 1: +3.3V -> D+3.3V
- C19 pad 2: GND -> GNDD
- C2 pad 2: GND -> GNDD
- C20 pad 2: GND -> GNDD
- C21 pad 1: +3.3V -> D+3.3V
- C21 pad 2: GND -> GNDD
- C22 pad 1: +3.3V -> D+3.3V
- C22 pad 2: GND -> GNDD
- C23 pad 1: GND -> A+12V
- C23 pad 2: X_LIMIT1 -> GNDA
- C24 pad 1: GND -> A+3.3V
- C24 pad 2: X_LIMIT2 -> GNDA
- C25 pad 1: GND -> X_LIMIT1
- C25 pad 2: Y_LIMIT1 -> GNDD
- C26 pad 1: GND -> X_LIMIT2
- C26 pad 2: Y_LIMIT2 -> GNDD
- C27 pad 1: DGND -> GNDA
- C27 pad 2: D33V -> A+3.3V
- C28 pad 1: GND -> Y_LIMIT1
- C28 pad 2: D_SWITCH -> GNDD
- C29 pad 1: D33V -> A+3.3V
- C29 pad 2: DGND -> GNDA
- C3 pad 2: GND -> GNDD
- C30 pad 1: +3.3V -> D+3.3V
- C30 pad 2: GND -> GNDD
- C31 pad 1: D33V -> A+3.3V
- C31 pad 2: DGND -> GNDA
- C32 pad 2: DGND -> GNDA
- C33 pad 2: DGND -> GNDA
- C34 pad 2: DGND -> GNDA
- C35 pad 1: DGND -> GNDA
- C35 pad 2: D12V -> A+12V
- C36 pad 1: DGND -> GNDA
- C36 pad 2: D12V -> A+12V
- C37 pad 1: D12V -> A+12V
- C37 pad 2: DGND -> GNDA
- C38 pad 1: D12V -> A+12V
- C38 pad 2: DGND -> GNDA
- C39 pad 1: D33V -> A+3.3V
- C39 pad 2: DGND -> GNDA
- C4 pad 1: D33V -> A+3.3V
- C4 pad 2: DGND -> GNDA
- C40 pad 2: D12V -> A+12V
- C41 pad 2: D12V -> A+12V
- C42 pad 1: D33V -> A+3.3V
- C42 pad 2: DGND -> GNDA
- C43 pad 1: D33V -> A+3.3V
- C43 pad 2: DGND -> GNDA
- C46 pad 2: DGND -> GNDA
- C47 pad 2: DGND -> GNDA
- C5 pad 1: D12V -> A+12V
- C5 pad 2: DGND -> GNDA
- C6 pad 1: +3.3V -> D+3.3V
- C6 pad 2: GND -> GNDD
- C7 pad 1: N-00000130 -> A+12V
- C7 pad 2: DGND -> GNDA
- C8 pad 1: D5V -> A+5V
- C8 pad 2: DGND -> GNDA
- C9 pad 2: GND -> GNDD
- D2 pad 1: D12V -> A+12V
- D3 pad 1: D33V -> A+3.3V
- D4 pad 1: D5V -> A+5V
- D5 pad 1: N-0000049 -> Net-(D5-Pad1)
- D5 pad 2: N-0000094 -> Net-(D5-Pad2)
- D6 pad 1: N-0000045 -> Net-(D6-Pad1)
- D6 pad 2: N-0000093 -> Net-(D6-Pad2)
- D7 pad 1: N-0000044 -> Net-(D7-Pad1)
- D7 pad 2: N-0000092 -> Net-(D7-Pad2)
- D8 pad 1: N-0000043 -> Net-(D8-Pad1)
- D8 pad 2: N-0000095 -> Net-(D8-Pad2)
- D9 pad 1: N-0000078 -> Net-(D9-Pad1)
- D9 pad 2: N-0000079 -> Net-(D9-Pad2)
- J1 pad 1: +3.3V -> D+3.3V
- J1 pad 3: GND -> GNDD
- J1 pad 5: GND -> GNDD
- J1 pad 9: GND -> GNDD
- J10 pad 1: N-0000095 -> Net-(D9-Pad2)
- J10 pad 2: DGND -> GNDA
- J11 pad 1: N-00000114 -> Net-(J11-Pad1)
- J11 pad 3: DGND -> GNDA
- J14 pad 1: Y_MOT_2B -> Y1_MOT_2B
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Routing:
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- added copper zone on In2.Cu, net A+12V
- added copper zone on In2.Cu, net D+3.3V
- added copper zone on B.Cu, net GNDA
- added copper zone on F.Cu, net GNDA
- added copper zone on In1.Cu, net GNDA
- added copper zone on B.Cu, net GNDD
- added copper zone on F.Cu, net GNDD
- added copper zone on In1.Cu, net GNDD
- removed copper zone on B.Cu, net +3.3V
- removed copper zone on F.Cu, net +3.3V
- removed copper zone on B.Cu, net D33V
- removed copper zone on F.Cu, net D33V
- removed copper zone on B.Cu, net D5V
- removed copper zone on F.Cu, net D5V
- removed copper zone on B.Cu, net DGND
- removed copper zone on F.Cu, net DGND
- removed copper zone on B.Cu, net GND
- removed copper zone on F.Cu, net GND
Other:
- board size 110.5 x 77 mm -> 139.5 x 77 mm
- copper layers 2 -> 4
- net class motor: trace_width 1.016 -> 1.026

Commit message: ver 2.0
- DFUモード用のLEDを追加
-フォトカプラ改修(GND接続)
- R28 R4 R65 パッドサイズを0603に変更
- 部品表 1k パッドサイズ1206→0603
-TPL0401 PADピッチ誤り修正（TO-SOT23-6→カスタムPAD）
-TP穴径変更
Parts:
- added D10: 3.3V, Diodes_SMD:D_0603, F.Cu at (224.7, 98.7)
- added R42: 470R, Resistors_SMD:R_0603, F.Cu at (228.5, 98.7)
- R28, R4, R65: footprint Resistors_SMD:R_1206 -> Resistors_SMD:R_0603
- TP1, TP2, TP3, TP4: footprint Pin_Headers:Pin_Header_Straight_1x01_Pitch1.00mm -> Pin_Headers:Pin_Header_Straight_1x01_Pitch2.54mm
- U23, U24: footprint TO_SOT_Packages_SMD:SOT-23-6 -> mylib:TPL0401
- moved R38 11.4 mm to (205.8, 143.4), turned to 180 degrees
- moved ? 1.57 mm to (224.7, 98.8)
- moved TP2 1.38 mm to (135.8, 153.7)
- moved TP3 1.30 mm to (267.8, 154.3)
- moved U23 1.12 mm to (205.0, 140.8), turned to 270 degrees
- moved U24 1.09 mm to (205.0, 135.8), turned to 270 degrees
- moved R65 0.72 mm to (204.5, 127.5)
- moved R4 0.68 mm to (266.9, 96.8)
- moved TP1 0.48 mm to (136.0, 96.8)
- moved R23 0.33 mm to (251.7, 136.5)
- moved TP4 0.32 mm to (266.9, 101.5)
- moved R18 0.30 mm to (257.2, 136.5)
- moved R20 0.23 mm to (246.1, 136.4)
- moved R28 0.22 mm to (138.7, 127.3)
- moved R19 0.20 mm to (262.6, 136.6)
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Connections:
- U10 pad 4: (no net) -> GNDD
- U18 pad 4: (no net) -> GNDD
- U22 pad 4: (no net) -> GNDD
- U7 pad 4: (no net) -> GNDD
- U8 pad 4: (no net) -> GNDD
- U9 pad 4: (no net) -> GNDD
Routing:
- net Net-(R29-Pad1): track 6.70 -> 12.8 mm, vias 0 -> 2
- net A+3.3V: track 319.3 -> 324.0 mm
- net Net-(D10-Pad2): track 0.00 -> 2.18 mm
- net D+3.3V: track 112.0 -> 113.9 mm
- net Net-(R38-Pad2): track 25.7 -> 27.6 mm
- net Net-(C33-Pad1): track 10.0 -> 10.7 mm
- net Net-(R36-Pad2): track 28.2 -> 27.5 mm
